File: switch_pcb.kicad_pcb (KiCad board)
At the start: 2 copper layers, 50 x 40 mm, 9 parts, among them J1 3x5mm, SW1 Microswitch

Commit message: Switch back to the previous circuit with switch at the top
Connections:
- R1 pad 1: +5V -> GND
- SW1 pad 1: GND -> +5V
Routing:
- net +5V: track 41.3 -> 23.0 mm
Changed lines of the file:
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@@
 			(layers "*.Cu" "*.Mask")
 			(remove_unused_layers no)
-			(net 1 "GND")
+			(net 5 "+5V")
 			(pinfunction "COM")
 			(pintype "passive")
@@
 		(tags "Resistor Axial_DIN0207 series Axial Horizontal pin pitch 10.16mm 0.25W = 1/4W length 6.3mm diameter 2.5mm")
 		(property "Reference" "R1"
-			(at 5.08 2.35 360)
+			(at 5.08 2.35 0)
 			(layer "F.SilkS")
 			(effects
@@
 		)
 		(property "Value" "???"
-			(at 5.08 2.37 360)
+			(at 5.08 2.37 0)
 			(layer "F.Fab")
 			(effects
@@
 		)
 		(fp_text user "${REFERENCE}"
-			(at 5.08 0 360)
+			(at 5.08 0 0)
 			(layer "F.Fab")
 			(effects
@@
 			(layers "*.Cu" "*.Mask")
 			(remove_unused_layers no)
-			(net 5 "+5V")
+			(net 1 "GND")
 			(pintype "passive")
 			(teardrops
@@
 	)
 	(segment
-		(start 168.181 113.75)
-		(end 141.25 113.75)
-		(width 1)
-		(layer "F.Cu")
-		(net 5)
-	)
-	(segment
-		(start 141.25 113.75)
+		(start 147.42 94.08)
 		(end 134.5 107)
 		(width 1)
@@
 	)
 	(segment
-		(start 171.581 110.35)
-		(end 168.181 113.75)
+		(start 147.42 89.37)
+		(end 147.42 94.08)
 		(width 1)
 		(layer "F.Cu")
 		(net 5)
+	)
+	(zone
+		(net 2)
+		(net_name "Net-(J1-Pin_2)")
+		(layer "F.Cu")
+		(name "$teardrop_padvia$")
+		(hatch full 0.1)
+		(priority 30005)
+		(attr
+			(teardrop
+				(type padvia)
+			)
+		)
+		(connect_pads yes
+			(clearance 0)
+		)
+		(min_thickness 0.0254)
+		(filled_areas_thickness no)
+		(fill yes
+			(thermal_gap 0.5)
+			(thermal_bridge_width 0.5)
+			(island_removal_mode 1)
+			(island_area_min 10)
+		)
+		(polygon
+			(pts
+				(xy 163.5 106) (xy 164.5 106) (xy 164.92388 104.382683) (xy 164 103.999) (xy 163.07612 104.382683)
+			)
+		)
+	)
+	(zone
+		(net 2)
+		(net_name "Net-(J1-Pin_2)")
+		(layer "F.Cu")
+		(name "$teardrop_padvia$")
+		(hatch full 0.1)
+		(priority 30007)
+		(attr
+			(teardrop
+				(type padvia)
+			)
+		)
+		(connect_pads yes
+			(clearance 0)
+		)
+		(min_thickness 0.0254)
+		(filled_areas_thickness no)
+		(fill yes
+			(thermal_gap 0.5)
+			(thermal_bridge_width 0.5)
+			(island_removal_mode 1)
+			(island_area_min 10)
+		)
+		(polygon
+			(pts
+				(xy 163.188168 109.288939) (xy 162.481061 108.581832) (xy 161.038317 109.42612) (xy 161.420293 110.350707)
+				(xy 162.34488 110.732683)
+			)
+		)
+	)
+	(zone
+		(net 2)
+		(net_name "Net-(J1-Pin_2)")
+		(layer "F.Cu")
+		(name "$teardrop_padvia$")
+		(hatch full 0.1)
+		(priority 30001)
+		(attr
+			(teardrop
+				(type padvia)
+			)
+		)
+		(connect_pads yes
+			(clearance 0)
+		)
+		(min_thickness 0.0254)
+		(filled_areas_thickness no)
+		(fill yes
+			(thermal_gap 0.5)
+			(thermal_bridge_width 0.5)
+			(island_removal_mode 1)
+			(island_area_min 10)
+		)
+		(polygon
+			(pts
+				(xy 140.762285 108.969392) (xy 141.469392 108.262285) (xy 140.775549 106.861335) (xy 139.499293 106.999293)
+				(xy 139.366036 108.28025)
+			)
+		)
+	)
+	(zone
+		(net 2)
+		(net_name "Net-(J1-Pin_2)")
+		(layer "F.Cu")
+		(name "$teardrop_padvia$")
+		(hatch full 0.1)
+		(priority 30004)
+		(attr
+			(teardrop
+				(type padvia)
+			)
+		)
+		(connect_pads yes
+			(clearance 0)
+		)
+		(min_thickness 0.0254)
+		(filled_areas_thickness no)
+		(fill yes
+			(thermal_gap 0.5)
+			(thermal_bridge_width 0.5)
+			(island_removal_mode 1)
+			(island_area_min 10)
+		)
+		(polygon
+			(pts
+				(xy 159.421 109.85) (xy 159.421 110.85) (xy 161.038317 111.27388) (xy 161.422 110.35) (xy 161.038317 109.42612)
+			)
+		)
+	)
+	(zone
+		(net 5)
+		(net_name "+5V")
+		(layer "F.Cu")
+		(name "$teardrop_padvia$")
+		(hatch full 0.1)
+		(priority 30002)
+		(attr
+			(teardrop
+				(type padvia)
+			)
+		)
+		(connect_pads yes
+			(clearance 0)
+		)
+		(min_thickness 0.0254)
+		(filled_areas_thickness no)
+		(fill yes
+			(thermal_gap 0.5)
+			(thermal_bridge_width 0.5)
+			(island_removal_mode 1)
+			(island_area_min 10)
+		)
+		(polygon
+			(pts
+				(xy 146.92 91.363089) (xy 147.92 91.363089) (xy 148.42 90.00704) (xy 147.42 89.369) (xy 146.42 90.00704)
+			)
+		)
+	)
+	(zone
+		(net 2)
+		(net_name "Net-(J1-Pin_2)")
+		(layer "F.Cu")
+		(name "$teardrop_padvia$")
+		(hatch full 0.1)
+		(priority 30006)
+		(attr
+			(teardrop
+				(type padvia)
+			)
+		)
+		(connect_pads yes
+			(clearance 0)
+		)
+		(min_thickness 0.0254)
+		(filled_areas_thickness no)
+		(fill yes
+			(thermal_gap 0.5)
+			(thermal_bridge_width 0.5)
+			(island_removal_mode 1)
+			(island_area_min 10)
+		)
+		(polygon
+			(pts
+				(xy 162.93934 102.232233) (xy 162.232233 102.93934) (xy 163.07612 104.382683) (xy 164.000707 104.000707)
+				(xy 164.382683 103.07612)
+			)
+		)
 	)
 	(zone
@@
 		(polygon
 			(pts
-				(xy 136.153553 109.36066) (xy 136.86066 108.653553) (xy 135.8 106.885786) (xy 134.499293 106.999293)
-				(xy 134.385787 108.3)
-			)
-		)
-	)
-	(zone
-		(net 2)
-		(net_name "Net-(J1-Pin_2)")
-		(layer "F.Cu")
-		(name "$teardrop_padvia$")
-		(hatch full 0.1)
-		(priority 30004)
-		(attr
-			(teardrop
-				(type padvia)
-			)
-		)
-		(connect_pads yes
-			(clearance 0)
-		)
-		(min_thickness 0.0254)
-		(filled_areas_thickness no)
-		(fill yes
-			(thermal_gap 0.5)
-			(thermal_bridge_width 0.5)
-			(island_removal_mode 1)
-			(island_area_min 10)
-		)
-		(polygon
-			(pts
-				(xy 163.5 106) (xy 164.5 106) (xy 164.92388 104.382683) (xy 164 103.999) (xy 163.07612 104.382683)
-			)
-		)
-	)
-	(zone
-		(net 2)
-		(net_name "Net-(J1-Pin_2)")
-		(layer "F.Cu")
-		(name "$teardrop_padvia$")
-		(hatch full 0.1)
-		(priority 30006)
-		(attr
-			(teardrop
-				(type padvia)
-			)
-		)
-		(connect_pads yes
-			(clearance 0)
-		)
-		(min_thickness 0.0254)
-		(filled_areas_thickness no)
-		(fill yes
-			(thermal_gap 0.5)
-			(thermal_bridge_width 0.5)
-			(island_removal_mode 1)
-			(island_area_min 10)
-		)
-		(polygon
-			(pts
-				(xy 162.93934 102.232233) (xy 162.232233 102.93934) (xy 163.07612 104.382683) (xy 164.000707 104.000707)
-				(xy 164.382683 103.07612)
-			)
-		)
-	)
-	(zone
-		(net 5)
-		(net_name "+5V")
-		(layer "F.Cu")
-		(name "$teardrop_padvia$")
-		(hatch full 0.1)
-		(priority 30005)
-		(attr
-			(teardrop
-				(type padvia)
-			)
-		)
-		(connect_pads yes
-			(clearance 0)
-		)
-		(min_thickness 0.0254)
-		(filled_areas_thickness no)
-		(fill yes
-			(thermal_gap 0.5)
-			(thermal_bridge_width 0.5)
-			(island_removal_mode 1)
-			(island_area_min 10)
-		)
-		(polygon
-			(pts
-				(xy 169.813233 111.41066) (xy 170.52034 112.117767) (xy 171.963683 111.27388) (xy 171.581707 110.349293)
-				(xy 170.65712 109.967317)
-			)
-		)
-	)
-	(zone
-		(net 2)
-		(net_name "Net-(J1-Pin_2)")
-		(layer "F.Cu")
-		(name "$teardrop_padvia$")
-		(hatch full 0.1)
-		(priority 30001)
-		(attr
-			(teardrop
-				(type padvia)
-			)
-		)
-		(connect_pads yes
-			(clearance 0)
-		)
-		(min_thickness 0.0254)
-		(filled_areas_thickness no)
-		(fill yes
-			(thermal_gap 0.5)
-			(thermal_bridge_width 0.5)
-			(island_removal_mode 1)
-			(island_area_min 10)
-		)
-		(polygon
-			(pts
-				(xy 140.762285 108.969392) (xy 141.469392 108.262285) (xy 140.775549 106.861335) (xy 139.499293 106.999293)
-				(xy 139.366036 108.28025)
+				(xy 136.86066 105.346447) (xy 136.153553 104.63934) (xy 134.385786 105.7) (xy 134.499293 107.000707)
+				(xy 135.8 107.114214)
 			)
 		)
@@
 		(attr
 			(teardrop
-				(type padvia)
-			)
-		)
-		(connect_pads yes
-			(clearance 0)
-		)
-		(min_thickness 0.0254)
-		(filled_areas_thickness no)
-		(fill yes
-			(thermal_gap 0.5)
-			(thermal_bridge_width 0.5)
-			(island_removal_mode 1)
-			(island_area_min 10)
-		)
-		(polygon
-			(pts
-				(xy 159.421 109.85) (xy 159.421 110.85) (xy 161.038317 111.27388) (xy 161.422 110.35) (xy 161.038317 109.42612)
-			)
-		)
-	)
-	(zone
-		(net 2)
-		(net_name "Net-(J1-Pin_2)")
-		(layer "F.Cu")
-		(name "$teardrop_padvia$")
-		(hatch full 0.1)
-		(priority 30007)
-		(attr
-			(teardrop
-				(type padvia)
-			)
-		)
-		(connect_pads yes
-			(clearance 0)
-		)
-		(min_thickness 0.0254)
-		(filled_areas_thickness no)
-		(fill yes
-			(thermal_gap 0.5)
-			(thermal_bridge_width 0.5)
-			(island_removal_mode 1)
-			(island_area_min 10)
-		)
-		(polygon
-			(pts
-				(xy 163.188168 109.288939) (xy 162.481061 108.581832) (xy 161.038317 109.42612) (xy 161.420293 110.350707)
-				(xy 162.34488 110.732683)
-			)
-		)
-	)
-	(zone
-		(net 2)
-		(net_name "Net-(J1-Pin_2)")
-		(layer "F.Cu")
-		(name "$teardrop_padvia$")
-		(hatch full 0.1)
-		(priority 30002)
-		(attr
-			(teardrop

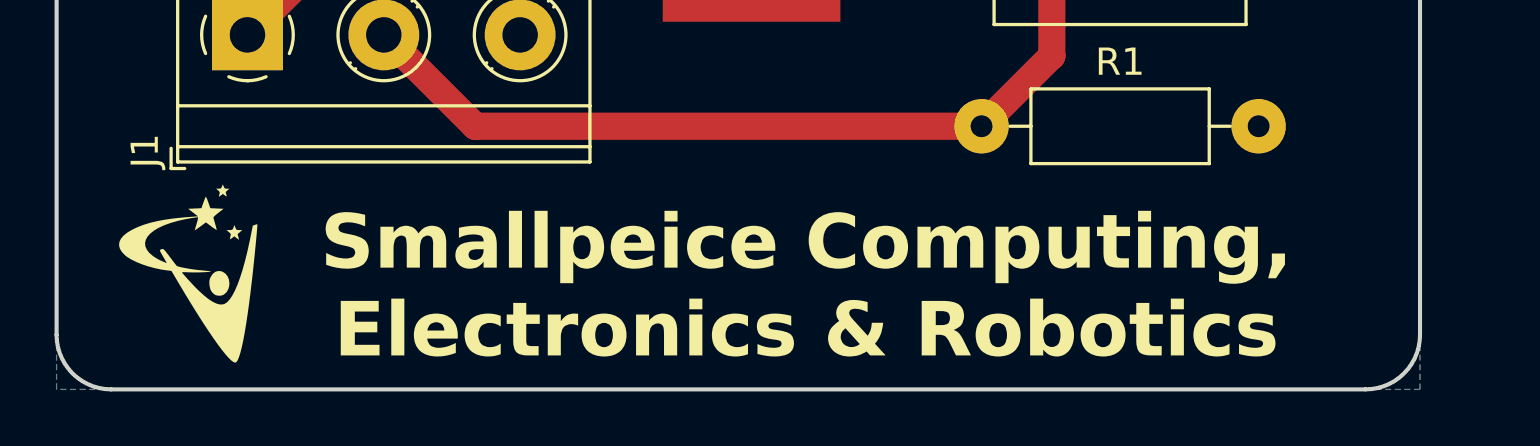
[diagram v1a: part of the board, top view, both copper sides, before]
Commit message: Update to "UoS Robotics Summer School" Switch to UoS logo Update to Kicad v9
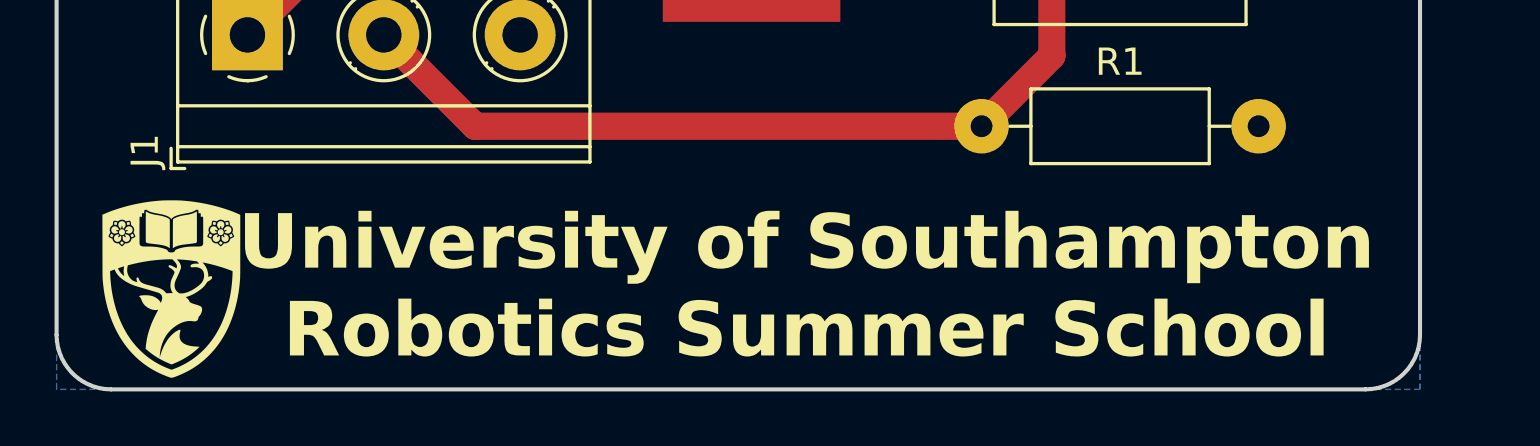
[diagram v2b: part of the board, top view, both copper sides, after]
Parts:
- G***: footprint switch_pcb:smallpeice -> switch_pcb:UoS
- moved G*** 1.46 mm to (131.8, 116.4)
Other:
- board text added: "SRO Extrusion Switch Mount WBB 1.1"
- board text added: "University of Southampton Robotics Summer School"
- board text removed: "SRO Extrusion Switch Mount WBB 1.0"
- board text removed: "Smallpeice Computing, Electronics & Robotics"

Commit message: Setup for serial number
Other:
- board text removed: "JLCJLCJLCJLC"
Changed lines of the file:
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@@
+		(layer "B.SilkS")
+	)
+	(gr_rect
+		(start 129 117)
+		(end 139 119)
+		(stroke
+			(width 0.15)
+			(type solid)
+		)
+		(fill yes)
 		(layer "B.SilkS")
 	)
@@
 		)
 	)
-	(gr_text "JLCJLCJLCJLC"
-		(at 128.75 118.5 0)
-		(layer "B.SilkS")
-		(effects
-			(font
-				(size 1 1)
-				(thickness 0.15)
-			)
-			(justify right bottom mirror)
-		)
-	)
